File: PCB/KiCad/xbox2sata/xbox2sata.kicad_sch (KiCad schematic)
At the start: 7 parts, among them J1 61203921621, J2 67800-8025, J3 90151-2140, U1 88SA8052, Y1 ABLS-25.000MHZ-B4-F-T

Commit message: PCB folder structure
Created two sub folders in PCB; Proteus and KiCad and moved respective files into folders.
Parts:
- J1: footprint 61203921621:WURTH-ELEKTRONIK_61203921621 -> xbox2sata:WURTH-ELEKTRONIK_61203921621
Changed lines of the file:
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@@
 			)
 		)
-		(property "Footprint" "61203921621:WURTH-ELEKTRONIK_61203921621"
+		(property "Footprint" "xbox2sata:WURTH-ELEKTRONIK_61203921621"
 			(at 126.238 98.044 0)
 			(effects

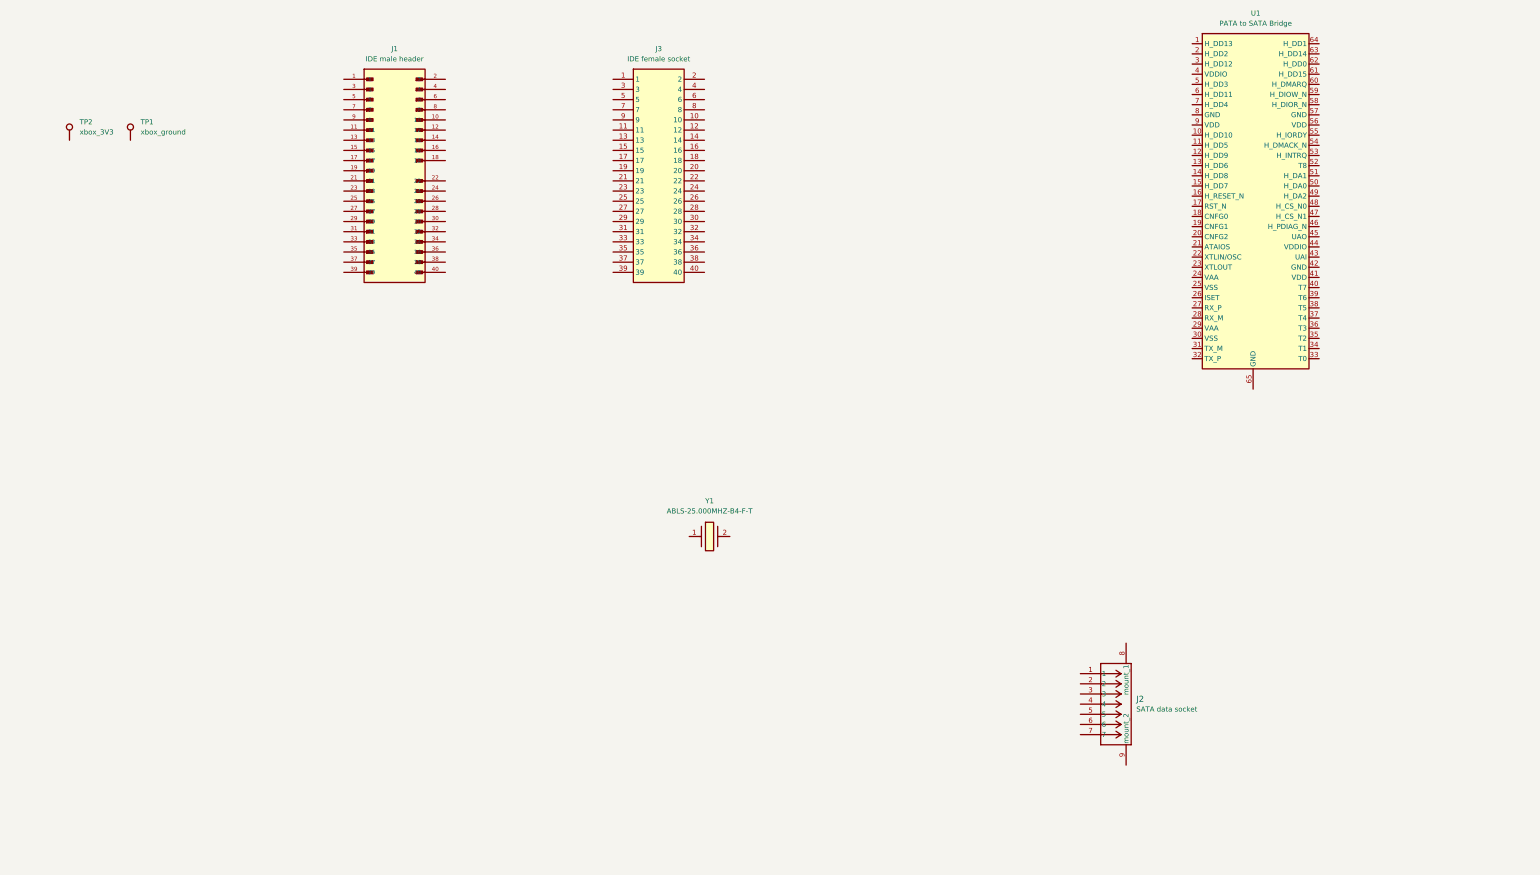
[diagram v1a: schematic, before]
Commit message: KiCad updates
Nets and some components added
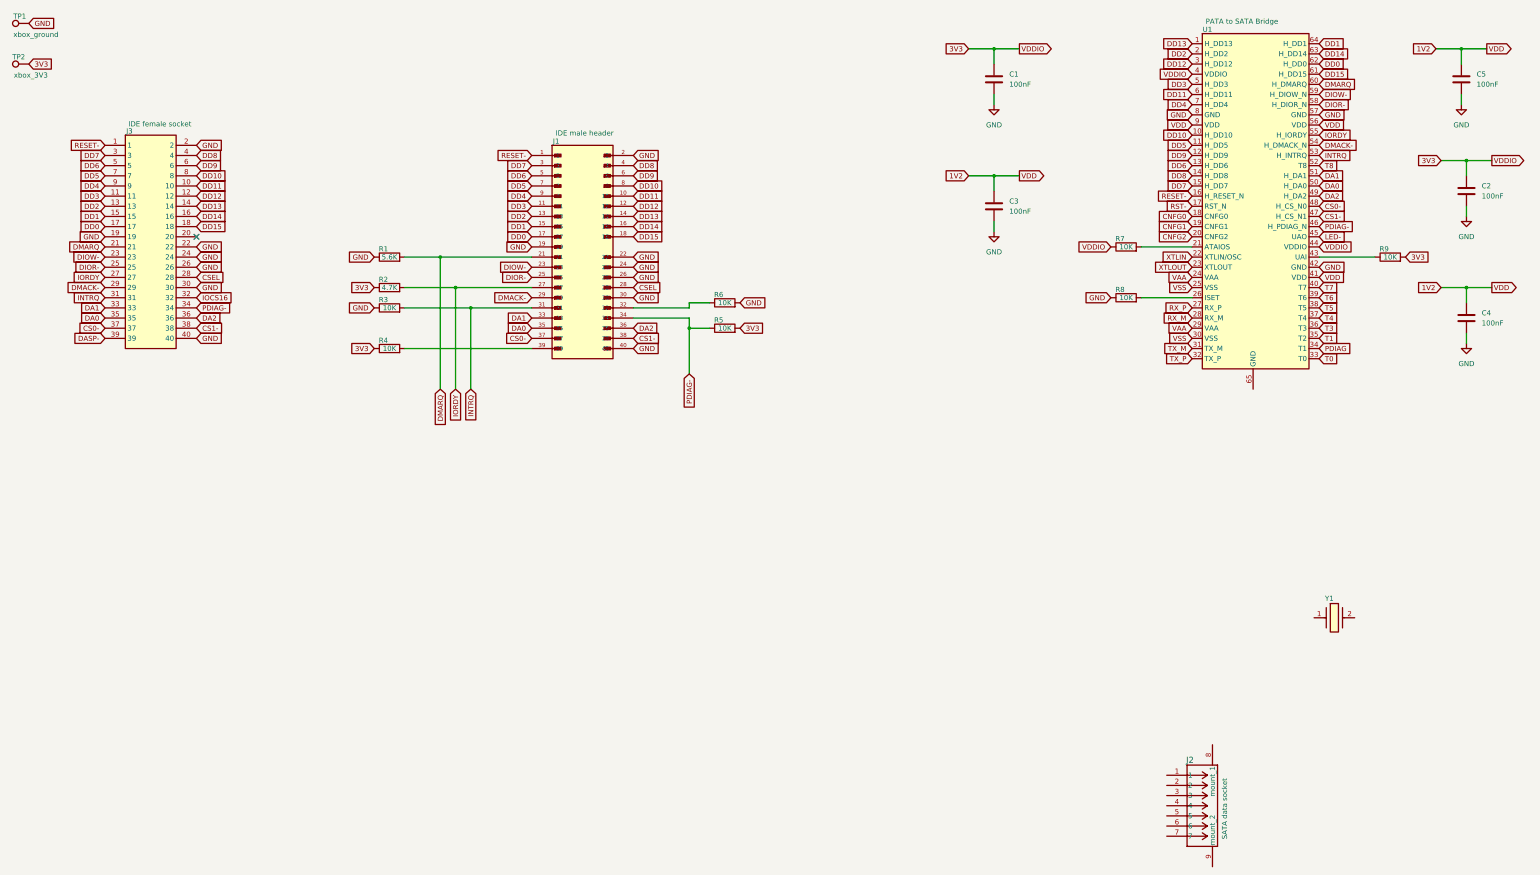
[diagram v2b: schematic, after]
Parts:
- added C1, C2, C3, C4, C5: 100nF, Capacitor_SMD:C_0402_1005Metric_Pad0.74x0.62mm_HandSolder, symbol Device:C
- added R1: 5.6K, Resistor_SMD:R_0402_1005Metric_Pad0.72x0.64mm_HandSolder, symbol Device:R
- added R2: 4.7K, Resistor_SMD:R_0402_1005Metric_Pad0.72x0.64mm_HandSolder, symbol Device:R
- added R3, R4, R5, R6, R7, R8, R9: 10K, Resistor_SMD:R_0402_1005Metric_Pad0.72x0.64mm_HandSolder, symbol Device:R
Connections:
- net RESET-: now reaches J3.1
- net RESET-: now also J1.1, U1.16 (H_RESET_N)
- net DD11: now reaches J3.10
- net DD11: now also J1.10, U1.6 (H_DD11)
- net DD3: now reaches J3.11
- net DD3: now also J1.11, U1.5 (H_DD3)
- net DD12: now reaches J3.12
- net DD12: now also J1.12, U1.3 (H_DD12)
- net DD2: now reaches J3.13
- net DD2: now also J1.13, U1.2 (H_DD2)
- net DD13: now reaches J3.14
- net DD13: now also J1.14, U1.1 (H_DD13)
- net DD1: now reaches J3.15
- net DD1: now also J1.15, U1.64 (H_DD1)
- net DD14: now reaches J3.16
- net DD14: now also J1.16, U1.63 (H_DD14)
- net DD0: now reaches J3.17
- net DD0: now also J1.17, U1.62 (H_DD0)
- net DD15: now reaches J3.18
- net DD15: now also J1.18, U1.61 (H_DD15)
- net GND: now reaches J3.19
- net GND: now also J1.19, J1.2, J1.22, J1.24, J1.26, J1.30, J1.40, J3.2, J3.22, J3.24, J3.26, J3.30, J3.40, TP1.1, U1.42 (GND), U1.57 (GND), U1.8 (GND), C1.2, C2.2, C3.2, C4.2, C5.2, R1.1, R3.1, R6.2, R8.1
- net DMARQ: now reaches J3.21
- net DMARQ: now also J1.21, U1.60 (H_DMARQ), R1.2
- net DIOW-: now reaches J3.23
- net DIOW-: now also J1.23, U1.59 (H_DIOW_N)
- net DIOR-: now reaches J3.25
- net DIOR-: now also J1.25, U1.58 (H_DIOR_N)
- net IORDY: now reaches J3.27
- net IORDY: now also J1.27, U1.55 (H_IORDY), R2.2
- net CSEL: now reaches J3.28
- net CSEL: now also J1.28
- net DMACK-: now reaches J3.29
- net DMACK-: now also J1.29, U1.54 (H_DMACK_N)
- net DD7: now reaches J3.3
- net DD7: now also J1.3, U1.15 (H_DD7)
- net INTRQ: now reaches J3.31
- net INTRQ: now also J1.31, U1.53 (H_INTRQ), R3.2
- net IOCS16: now reaches J3.32
- net DA1: now reaches J3.33
- net DA1: now also J1.33, U1.51 (H_DA1)
- net PDIAG-: now reaches J3.34
- net PDIAG-: now also J1.34, U1.46 (H_PDIAG_N), R5.1
- net DA0: now reaches J3.35
- net DA0: now also J1.35, U1.50 (H_DA0)
- net DA2: now reaches J3.36
- net DA2: now also J1.36, U1.49 (H_DA2)
- net CS0-: now reaches J3.37
- net CS0-: now also J1.37, U1.48 (H_CS_N0)
- net CS1-: now reaches J3.38
- net CS1-: now also J1.38, U1.47 (H_CS_N1)
- net DASP-: now reaches J3.39
- net DD8: now reaches J3.4
- net DD8: now also J1.4, U1.14 (H_DD8)
- net DD6: now reaches J3.5
- net DD6: now also J1.5, U1.13 (H_DD6)
- net DD9: now reaches J3.6
- net DD9: now also J1.6, U1.12 (H_DD9)
- net DD5: now reaches J3.7
- net DD5: now also J1.7, U1.11 (H_DD5)
- net DD10: now reaches J3.8
- net DD10: now also J1.8, U1.10 (H_DD10)
- net DD4: now reaches J3.9
- net DD4: now also J1.9, U1.7 (H_DD4)
- net RST-: now reaches U1.17 (RST_N)
- net CNFG0: now reaches U1.18 (CNFG0)
- net CNFG1: now reaches U1.19 (CNFG1)
- net CNFG2: now reaches U1.20 (CNFG2)
- net at U1.21 (ATAIOS): now also R7.2
- net XTLIN: now reaches U1.22 (XTLIN/OSC)
- net XTLOUT: now reaches U1.23 (XTLOUT)
- net VAA: now reaches U1.24 (VAA)
- net VAA: now also U1.29 (VAA)
- net VSS: now reaches U1.25 (VSS)
- net VSS: now also U1.30 (VSS)
- net at U1.26 (ISET): now also R8.2
- net RX_P: now reaches U1.27 (RX_P)
- net RX_M: now reaches U1.28 (RX_M)
- net TX_M: now reaches U1.31 (TX_M)
- net TX_P: now reaches U1.32 (TX_P)
- net T0: now reaches U1.33 (T0)
- net PDIAG: now reaches U1.34 (T1)
- net T1: now reaches U1.35 (T2)
- net T3: now reaches U1.36 (T3)
- net T4: now reaches U1.37 (T4)
- net T5: now reaches U1.38 (T5)
- net T6: now reaches U1.39 (T6)
- net 3V3: now reaches U1.4 (VDDIO)
- net 3V3: now also TP2.1, U1.44 (VDDIO), C1.1, C2.1, R2.1, R4.1, R5.2, R7.1, R9.2
- net T7: now reaches U1.40 (T7)
- net 1V2: now reaches U1.41 (VDD)
- net 1V2: now also U1.56 (VDD), U1.9 (VDD), C3.1, C4.1, C5.1
- net at U1.43 (UAI): now also R9.1
- net LED-: now reaches U1.45 (UAO)
- net T8: now reaches U1.52 (T8)
- net at J1.32: now also R6.1
- net at J1.39: now also R4.2
- no-connect marks 0 -> 1
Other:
- moved on the sheet: J1, J2, J3, TP1, TP2, Y1

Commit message: KiCad update
Added to schematic and pcb
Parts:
- added C10, C11, C12, C13: 10nF, Resistor_SMD:R_0402_1005Metric_Pad0.72x0.64mm_HandSolder, symbol Device:C
- added C14, C17: 10nF, Capacitor_SMD:C_0402_1005Metric_Pad0.74x0.62mm_HandSolder, symbol Device:C
- added C15, C16: 100nF, Capacitor_SMD:C_0402_1005Metric_Pad0.74x0.62mm_HandSolder, symbol Device:C
- added C6, C7: 1uF, Capacitor_SMD:C_0603_1608Metric_Pad1.08x0.95mm_HandSolder, symbol Device:C
- added C8, C9: 18pF, Capacitor_SMD:C_0402_1005Metric_Pad0.74x0.62mm_HandSolder, symbol Device:C
- added IC1: TLV1117LV12DCYR, xbox2sata:SOT230P700X180-4N, symbol xbox2sata:TLV1117LV12DCYR
- added L1: L, Inductor_SMD:L_0402_1005Metric_Pad0.77x0.64mm_HandSolder, symbol Device:L
- added R10: 1M, Resistor_SMD:R_0402_1005Metric_Pad0.72x0.64mm_HandSolder, symbol Device:R
- added R11: 100, Resistor_SMD:R_0402_1005Metric_Pad0.72x0.64mm_HandSolder, symbol Device:R
- added R12, R13, R14, R16, R17, R18: 10K, Resistor_SMD:R_0402_1005Metric_Pad0.72x0.64mm_HandSolder, symbol Device:R
- added R15: 4.7K, Resistor_SMD:R_0402_1005Metric_Pad0.72x0.64mm_HandSolder, symbol Device:R
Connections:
- net T4 is gone; now on net GND: U1.37 (T4)
- net 1V2: now also C6.1, IC1.2 (OUTPUT_1), IC1.4 (OUTPUT_2)
- net 3V3: now also C14.1, C7.1, IC1.3 (INPUT), L1.1, R13.2, R14.2, R16.1, R17.1
- net CNFG0: now also R12.1
- net CNFG1: now also R13.1
- net CNFG2: now also R14.1
- net GND: now also J2.1, J2.4, J2.7, J2.8 (mount_1), J2.9 (mount_2), C14.2, C6.2, C7.2, C8.2, C9.2, IC1.1 (GND), R12.2, R15.2, R18.1
- net RX_M: now also C11.1
- net RX_P: now also C13.1
- net T0: now also R15.1
- net T3: now also R16.2
- net T7: now also R17.2
- net T8: now also R18.2
- net TX_M: now also C12.1
- net TX_P: now also C10.1
- net VAA: now also C15.1, C16.1, C17.1, L1.2
- net VSS: now also C15.2, C16.2, C17.2
- net XTLIN: now also Y1.2, C9.1, R10.2
- net XTLOUT: now also R11.1
- net at J2.2: now also C10.2
- net at J2.3: now also C11.2
- net at J2.5: now also C12.2
- net at J2.6: now also C13.2
- net at Y1.1: now also C8.1, R10.1, R11.2
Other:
- moved on the sheet: J1, J3, R1, R2, R3, R4, R5, R6, Y1

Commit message: Notes added to KiCad schematic
Requests for checking routing and signals are correct.
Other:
- note added: "Are capacitors or resistors better for reflections in paired signals like these?"
- note added: "Information about CNFG and T setup from \documents\asus_f70sl_rev_1.0_sch.pdf"
- note added: "Is this regulator configuration OK? From datasheet \docs\datasheets\tlv1117lv.pdf"
- note added: "Please check IC connections using \images\Startech PCB layers.xcf and \documents\Startech IDE2SATA.PDF"
- note added: "Please check these are correct signals from xbox ide header."
- note added: "Please check these signals are traced correct from Startech PCB layers.xcf and if CSEL should be connected."
- note added: "Please measure original L1 or suggest a value. I am unfamiliar with this power filter circtuit, is it OK?"
- note added: "this site documents pins 15 and 9 on the LPC debug port supplies 3V3. https://xboxdevwiki.net/LPC_Debug_Port"
- moved on the sheet: C1, C10, C11, C12, C13, C14, C15, C16, C17, C2, C3, C4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

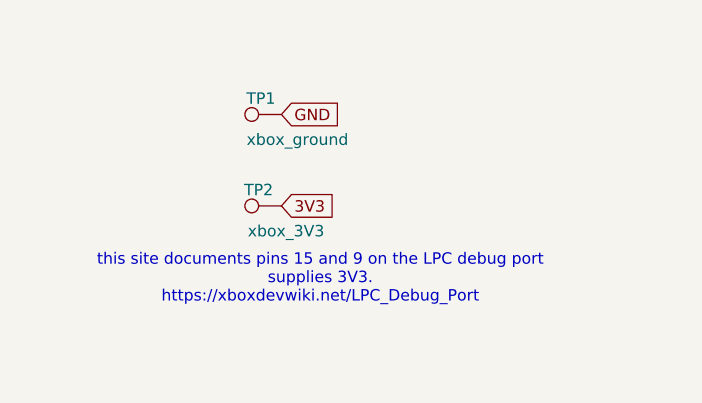
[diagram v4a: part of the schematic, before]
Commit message: ground cable point removed
ground to xbox through ide header
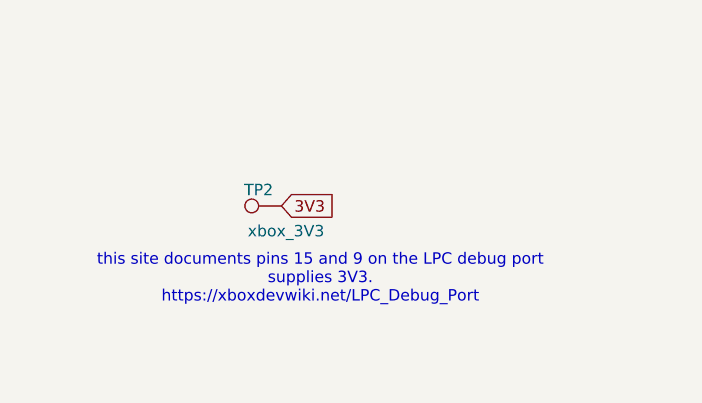
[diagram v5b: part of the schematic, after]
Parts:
- removed TP1: xbox_ground, TestPoint:TestPoint_THTPad_2.5x2.5mm_Drill1.2mm, symbol Connector:TestPoint
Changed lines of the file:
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@@
 		)
 	)
-	(global_label "GND"
-		(shape input)
-		(at 36.83 35.56 0)
-		(fields_autoplaced yes)
-		(effects
-			(font
-				(size 1.27 1.27)
-			)
-			(justify left)
-		)
-		(property "Intersheetrefs" "${INTERSHEET_REFS}"
-			(at 43.6857 35.56 0)
-			(effects
-				(font
-					(size 1.27 1.27)
-				)
-				(justify left)
-				(hide yes)
-			)
-		)
-	)
 	(global_label "DD12"
 		(shape input)
@@
 					(unit 1)
 				)
-			)
-		)
-	)
-	(symbol
-		(lib_id "Connector:TestPoint")
-		(at 36.83 35.56 90)
-		(unit 1)
-		(exclude_from_sim no)
-		(in_bom yes)
-		(on_board yes)
-		(dnp no)
-		(property "Reference" "TP1"
-			(at 34.544 33.782 90)
-			(effects
-				(font
-					(size 1.27 1.27)
-				)
-			)
-		)
-		(property "Value" "xbox_ground"
-			(at 38.608 38.354 90)
-			(effects
-				(font
-					(size 1.27 1.27)
-				)
-			)
-		)
-		(property "Footprint" "TestPoint:TestPoint_THTPad_2.5x2.5mm_Drill1.2mm"
-			(at 36.83 30.48 0)
-			(effects
-				(font
-					(size 1.27 1.27)
-				)
-				(hide yes)
-			)
-		)
-		(property "Datasheet" "~"
-			(at 36.83 30.48 0)
-			(effects
-				(font
-					(size 1.27 1.27)
-				)
-				(hide yes)
-			)
-		)
-		(property "Description" "test point"
-			(at 36.83 35.56 0)
-			(effects
-				(font
-					(size 1.27 1.27)
-				)
-				(hide yes)
-			)
-		)
-		(pin "1"
-		)
-		(instances
-			(project "xbox2sata"
-				(path "/29cbf96f-e8a1-446a-9b4f-b577bf6e6f05"
-					(reference "TP1")
-					(unit 1)
-				)

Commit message: slight changes to schematic
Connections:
- net GND: now also U1.65 (GND)
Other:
- title: (none) -> xbox2sata
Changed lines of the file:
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@@
 	(generator_version "8.0")
 	(paper "A3")
+	(title_block
+		(title "xbox2sata")
+	)
 	(junction
 		(at 260.35 261.62)
@@
 	(wire
 		(pts
+			(xy 328.93 129.54) (xy 328.93 132.08)
+		)
+		(stroke
+			(width 0)
+			(type default)
+		)
+	)
+	(wire
+		(pts
 			(xy 237.49 251.46) (xy 242.57 251.46)
 		)
@@
 	)
 	(symbol
+		(lib_id "power:GND")
+		(at 328.93 132.08 0)
+		(unit 1)
+		(exclude_from_sim no)
+		(in_bom yes)
+		(on_board yes)
+		(dnp no)
+		(fields_autoplaced yes)
+		(property "Reference" "#PWR014"
+			(at 328.93 138.43 0)
+			(effects
+				(font
+					(size 1.27 1.27)
+				)
+				(hide yes)
+			)
+		)
+		(property "Value" "GND"
+			(at 328.93 137.16 0)
+			(effects
+				(font
+					(size 1.27 1.27)
+				)
+			)
+		)
+		(property "Footprint" ""
+			(at 328.93 132.08 0)
+			(effects
+				(font
+					(size 1.27 1.27)
+				)
+				(hide yes)
+			)
+		)
+		(property "Datasheet" ""
+			(at 328.93 132.08 0)
+			(effects
+				(font
+					(size 1.27 1.27)
+				)
+				(hide yes)
+			)
+		)
+		(property "Description" "Power symbol creates a global label with name \"GND\" , ground"
+			(at 328.93 132.08 0)
+			(effects
+				(font
+					(size 1.27 1.27)
+				)
+				(hide yes)
+			)
+		)
+		(pin "1"
+		)
+		(instances
+			(project ""
+				(path "/29cbf96f-e8a1-446a-9b4f-b577bf6e6f05"
+					(reference "#PWR014")
+					(unit 1)
+				)
+			)
+		)
+	)
+	(symbol
 		(lib_id "Device:C")
 		(at 246.38 257.81 90)
@@
 					(unit 1)
 				)
+			)
+		)
+	)
+	(symbol
+		(lib_id "power:GND")
+		(at 273.05 85.09 0)
+		(unit 1)
+		(exclude_from_sim no)
+		(in_bom yes)
+		(on_board yes)
+		(dnp no)
+		(fields_autoplaced yes)
+		(property "Reference" "#PWR013"
+			(at 273.05 91.44 0)
+			(effects
+				(font
+					(size 1.27 1.27)
+				)
+				(hide yes)
+			)
+		)
+		(property "Value" "GND"
+			(at 273.05 90.17 0)
+			(effects
+				(font
+					(size 1.27 1.27)
+				)
+			)
+		)
+		(property "Footprint" ""
+			(at 273.05 85.09 0)
+			(effects
+				(font
+					(size 1.27 1.27)
+				)
+				(hide yes)
+			)
+		)
+		(property "Datasheet" ""
+			(at 273.05 85.09 0)
+			(effects
+				(font
+					(size 1.27 1.27)
+				)
+				(hide yes)
+			)
+		)
+		(property "Description" "Power symbol creates a global label with name \"GND\" , ground"
+			(at 273.05 85.09 0)
+			(effects
+				(font
+					(size 1.27 1.27)
+				)
+				(hide yes)
+			)
+		)
+		(pin "1"
+		)
+		(instances
+			(project ""
+				(path "/29cbf96f-e8a1-446a-9b4f-b577bf6e6f05"
+					(reference "#PWR013")
+					(unit 1)
+				)
